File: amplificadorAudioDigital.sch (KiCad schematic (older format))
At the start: 4 parts, among them U5 MAX98357A

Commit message: Esquema corregido, PCB terminada
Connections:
- net GAIN_SLOT: now reaches R4.1, U5.2 (GAIN_SLOT)
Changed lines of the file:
@@
 EESchema Schematic File Version 4
+LIBS:tpFinal-cache
 EELAYER 26 0
 EELAYER END
@@
 encoding utf-8
 Sheet 5 6
-Title ""
-Date ""
-Rev ""
-Comp ""
+Title "Sistema de comunicación en tiempo real por mensajes de voz
+"
+Date "2018-10-16"
+Rev "1.0"
+Comp "Marcelo Pistarelli"
 Comment1 ""
 Comment2 ""
@@
 Connection ~ 4700 4100
 Wire Wire Line
-	4700 2950 4100 2950
-Wire Wire Line
-	4100 2950 4100 3100
-Wire Wire Line
 	4100 3400 4100 3500
 Connection ~ 4100 3500
-Text HLabel 3950 2550 0    50   Input ~ 0
+Text HLabel 3100 2550 0    50   Input ~ 0
 Din
-Text HLabel 3950 2700 0    50   Input ~ 0
+Text HLabel 3100 2700 0    50   Input ~ 0
 SD_MODE
-Text HLabel 3950 2850 0    50   Input ~ 0
+Text HLabel 3100 2850 0    50   Input ~ 0
 BCLK
-Text HLabel 3950 3000 0    50   Input ~ 0
+Text HLabel 3100 3000 0    50   Input ~ 0
 LRCLK
 Text HLabel 6150 2850 2    50   Output ~ 0
@@
 Wire Wire Line
 	5900 2950 6150 2950
-Wire Wire Line
-	4700 3250 4550 3250
-Wire Wire Line
-	4550 3250 4550 3000
-Wire Wire Line
-	4550 3000 3950 3000
-Wire Wire Line
-	4700 3150 4600 3150
-Wire Wire Line
-	4600 3150 4600 2850
-Wire Wire Line
-	4600 2850 3950 2850
-Wire Wire Line
-	4700 3050 4650 3050
-Wire Wire Line
-	4650 3050 4650 2700
-Wire Wire Line
-	4650 2700 3950 2700
-Wire Wire Line
-	3950 2550 4700 2550
-Wire Wire Line
-	4700 2550 4700 2850
-Text HLabel 3650 3500 0    50   Input ~ 0
+Text HLabel 3050 3500 0    50   Input ~ 0
 Vdd
-Text HLabel 3650 4100 0    50   Input ~ 0
+Text HLabel 3050 4100 0    50   Input ~ 0
 GND
 Wire Wire Line
-	3650 4100 4100 4100
+	3050 4100 4100 4100
 Connection ~ 4100 4100
 Wire Wire Line
-	3650 3500 4100 3500
+	3050 3500 4100 3500
+Text Label 3200 2550 0    50   ~ 0
+Din
+Text Label 4600 2850 2    50   ~ 0
+Din
+Text Label 3200 2700 0    50   ~ 0
+SD_MODE
+Text Label 4600 3050 2    50   ~ 0
+SD_MODE
+Text Label 3200 2850 0    50   ~ 0
+BCLK
+Text Label 4600 3150 2    50   ~ 0
+BCLK
+Text Label 3200 3000 0    50   ~ 0
+LRCLK
+Text Label 4600 3250 2    50   ~ 0
+LRCLK
+Text Label 4600 2950 2    50   ~ 0
+GAIN_SLOT
+Text Label 4000 3100 2    50   ~ 0
+GAIN_SLOT
+Wire Wire Line
+	3100 2550 3200 2550
+Wire Wire Line
+	3100 2700 3200 2700
+Wire Wire Line
+	3100 2850 3200 2850
+Wire Wire Line
+	3100 3000 3200 3000
+Wire Wire Line
+	4600 2850 4700 2850
+Wire Wire Line
+	4600 2950 4700 2950
+Wire Wire Line
+	4600 3050 4700 3050
+Wire Wire Line
+	4600 3150 4700 3150
+Wire Wire Line
+	4600 3250 4700 3250
+Wire Wire Line
+	4000 3100 4100 3100
 $EndSCHEMATC

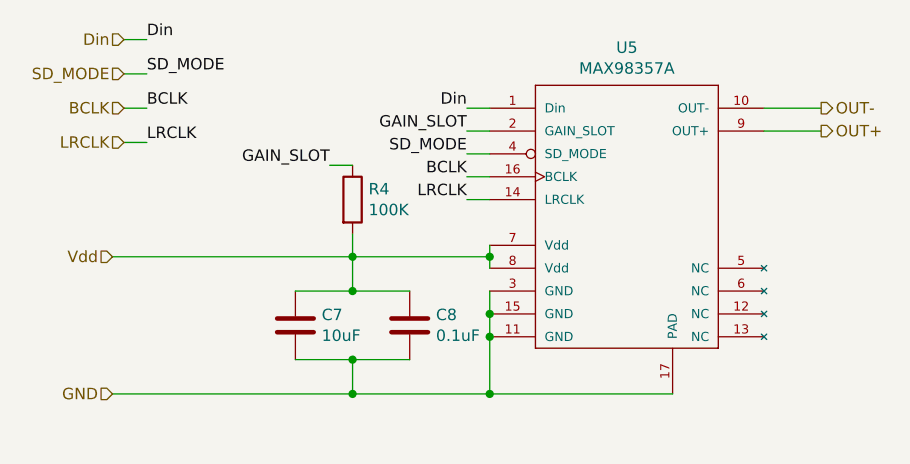
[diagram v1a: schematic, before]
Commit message: Se aplicaron correciones indicadas por el profesor en el esquemático
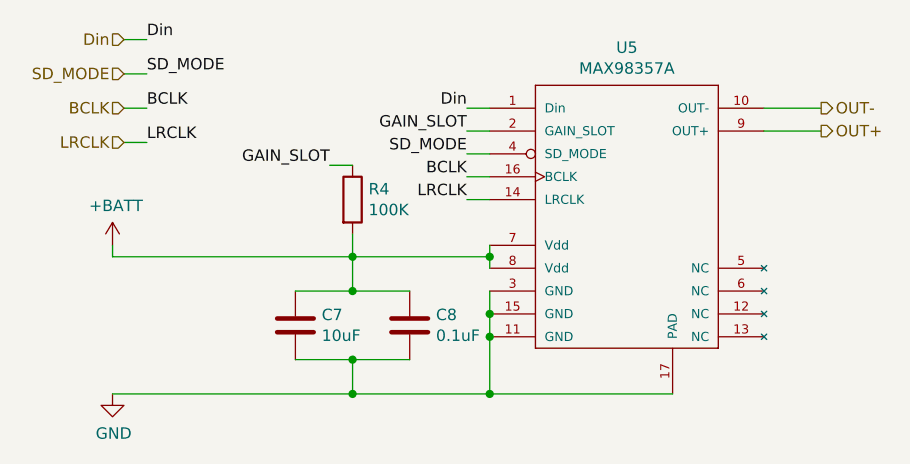
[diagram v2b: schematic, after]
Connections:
- net Vdd renamed +BATT
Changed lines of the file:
@@
 $Descr A4 11693 8268
 encoding utf-8
-Sheet 5 6
+Sheet 2 4
 Title "Sistema de comunicación en tiempo real por mensajes de voz
 "
@@
 Rev "1.0"
 Comp "Marcelo Pistarelli"
-Comment1 ""
+Comment1 "<C> 2018 Todos los derechos reservados"
 Comment2 ""
 Comment3 ""
@@
 Wire Wire Line
 	5900 2950 6150 2950
-Text HLabel 3050 3500 0    50   Input ~ 0
-Vdd
-Text HLabel 3050 4100 0    50   Input ~ 0
-GND
 Wire Wire Line
 	3050 4100 4100 4100
@@
 Wire Wire Line
 	4000 3100 4100 3100
+$Comp
+L power:GND #PWR0101
+U 1 1 5BFA97DD
+P 3050 4100
+F 0 "#PWR0101" H 3050 3850 50  0001 C CNN
+F 1 "GND" H 3055 3927 50  0000 C CNN
+F 2 "" H 3050 4100 50  0001 C CNN
+F 3 "" H 3050 4100 50  0001 C CNN
+	1    3050 4100
+	1    0    0    -1
+$EndComp
+$Comp
+L power:+BATT #PWR?
+U 1 1 5BFAC44C
+P 3050 3450
+AR Path="/5BFAC44C" Ref="#PWR?"  Part="1"
+AR Path="/5BC61204/5BFAC44C" Ref="#PWR0102"  Part="1"
+F 0 "#PWR0102" H 3050 3300 50  0001 C CNN
+F 1 "+BATT" H 3065 3623 50  0000 C CNN
+F 2 "" H 3050 3450 50  0001 C CNN
+F 3 "" H 3050 3450 50  0001 C CNN
+	1    3050 3450
+	1    0    0    -1
+$EndComp
+Wire Wire Line
+	3050 3450 3050 3500
 $EndSCHEMATC
